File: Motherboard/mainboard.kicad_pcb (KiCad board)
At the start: 4 copper layers, 45 x 35 mm, 48 parts, among them IC1 BMX160, J1 Conn_01x01, J2 10118194-0001LF, J28 Conn_01x01, J29 Conn_01x01, J3 Micro_SD_Card, J30 Conn_01x01, J4 xf2m-2415-1a, J5 XF2M-1015-1A, SW1 KMR231NG LFS, U1 RFM95W-915S2, U2 ATSAMD51G_TQFN48, U3 DRV8848, U4 TPS82740BSIPR, U5 DRV8848, U6 MAX708RESA-T, U8 RFM95W-915S2, X1 ANTENNA_U.FL, X2 ANTENNA_U.FL

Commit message: put top layer back in after accidentally deleting it....
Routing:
- net +3V3: track 20.1 -> 21.6 mm, vias 15 -> 16
- added copper zone on F.Cu, net GND

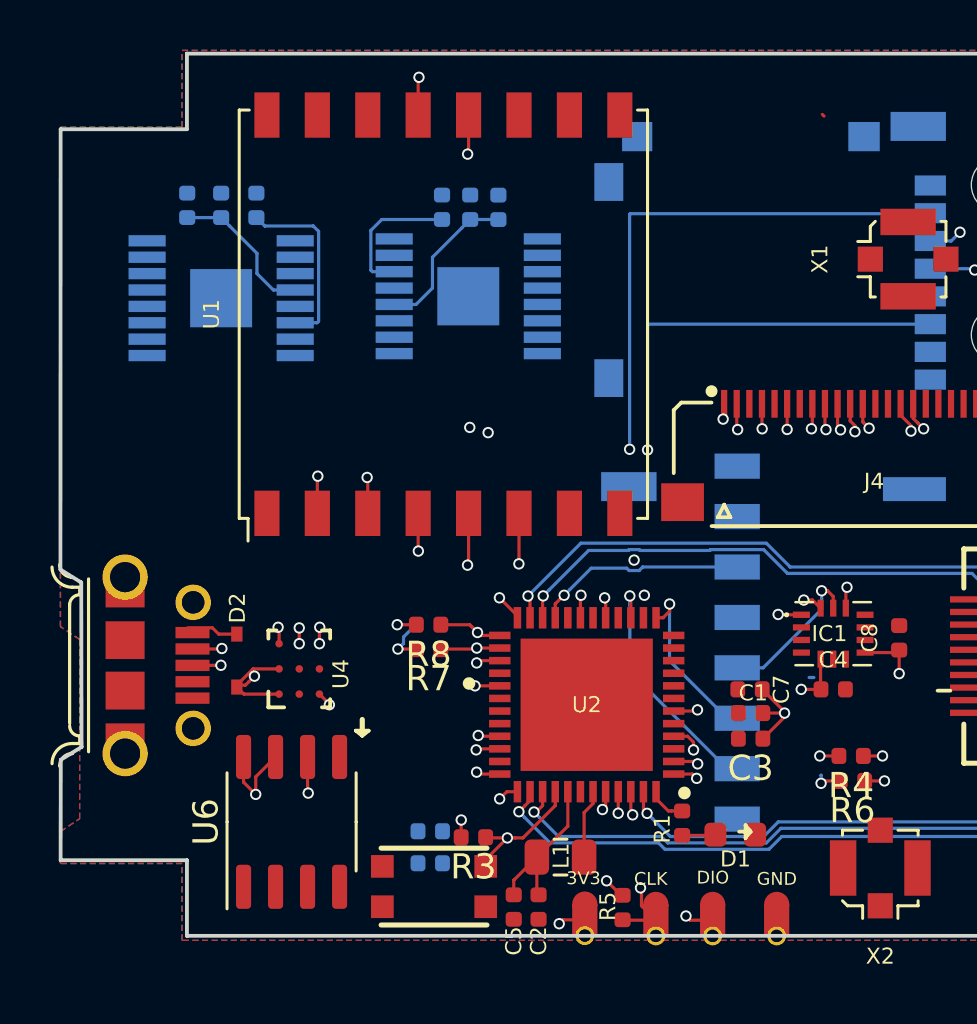
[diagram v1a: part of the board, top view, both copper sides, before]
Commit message: updated H-bridge voltage nests on schematic, updated traces on PCB for H-bridges to flat flex connector and for watchdog timer
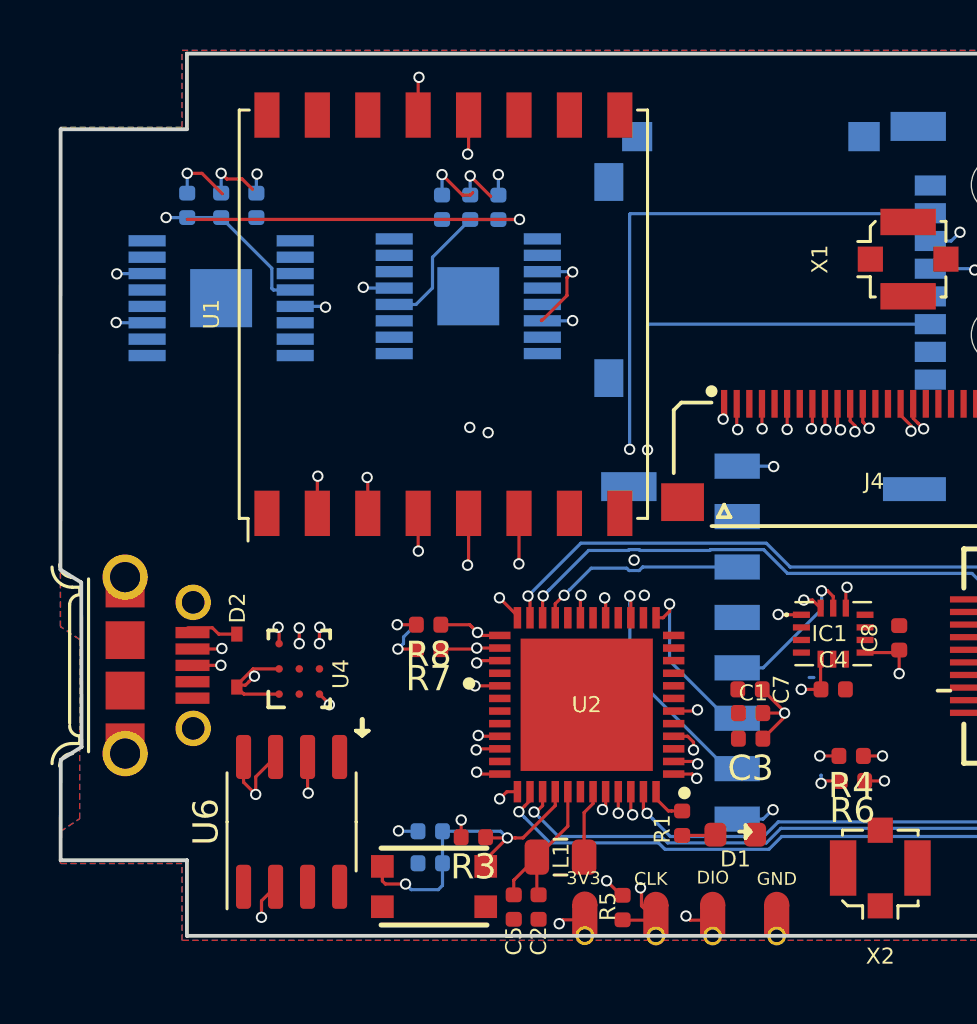
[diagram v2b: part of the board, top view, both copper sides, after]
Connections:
- C10 pad 1: Net-(C10-Pad1) -> BATT_P
- C11 pad 2: Net-(C11-Pad2) -> 3V3
- C12 pad 1: Net-(C12-Pad1) -> BATT_P
- C13 pad 2: Net-(C13-Pad2) -> 3V3
- C14 pad 1: Net-(C12-Pad1) -> BATT_P
- C9 pad 1: Net-(C10-Pad1) -> BATT_P
- U3 pad 11: VINT_1 -> 3V3
- U3 pad 12: Net-(C10-Pad1) -> BATT_P
- U3 pad 14: Net-(C11-Pad2) -> 3V3
- U5 pad 11: VINT_1 -> 3V3
- U5 pad 12: Net-(C12-Pad1) -> BATT_P
- U5 pad 14: Net-(C13-Pad2) -> 3V3
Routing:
- net BATT_P: track 13.9 -> 83.9 mm, vias 2 -> 4
- net GND: track 2.76 -> 27.4 mm, vias 2 -> 17
- net ~RESET: track 5.69 -> 13.7 mm, vias 1 -> 2
- net Net-(C13-Pad2): track 7.21 -> 0.00 mm
- net Net-(C10-Pad1): track 6.24 -> 0.00 mm
- net Net-(C12-Pad1): track 5.94 -> 0.00 mm
- net Net-(C11-Pad2): track 5.53 -> 0.00 mm
- net +3V3: track 21.6 -> 23.4 mm, vias 16 -> 17

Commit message: finished final touches for motherboard first draft
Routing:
- net BATT_P: track 83.9 -> 70.8 mm
- net 3V3: track 0.00 -> 2.23 mm, vias 0 -> 1
- net ~RESET: track 13.7 -> 15.0 mm
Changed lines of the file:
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@@
     (thickness 1.2)
     (drawings 35)
-    (tracks 629)
+    (tracks 634)
     (zones 0)
     (modules 48)
@@
   )
   (layers
-    (0 Top power hide)
-    (1 In1.Cu mixed)
+    (0 Top power)
+    (1 In1.Cu mixed hide)
     (2 In2.Cu mixed hide)
     (31 Bottom power)
@@
   (segment (start 91.86404 104.89184) (end 94.17304 104.89184) (width 0.127) (layer Bottom) (net 63))
   (segment (start 91.86404 105.74184) (end 91.86404 104.89184) (width 0.127) (layer Bottom) (net 63))
-  (via (at 90.3986 106.9848) (size 0.45) (drill 0.3) (layers Top Bottom) (net 63))
-  (segment (start 89.6003 106.9848) (end 90.3986 106.9848) (width 0.127) (layer Top) (net 63))
-  (segment (start 89.4789 106.8634) (end 89.6003 106.9848) (width 0.127) (layer Top) (net 63))
-  (segment (start 89.4789 106.2864) (end 89.4789 106.8634) (width 0.127) (layer Top) (net 63))
-  (segment (start 90.623599 107.209799) (end 91.697601 107.209799) (width 0.127) (layer Bottom) (net 63))
-  (segment (start 90.3986 106.9848) (end 90.623599 107.209799) (width 0.127) (layer Bottom) (net 63))
-  (segment (start 91.86404 107.04336) (end 91.86404 106.16184) (width 0.127) (layer Bottom) (net 63))
-  (segment (start 91.697601 107.209799) (end 91.86404 107.04336) (width 0.127) (layer Bottom) (net 63))
+  (via (at 91.8464 106.9086) (size 0.45) (drill 0.3) (layers Top Bottom) (net 63))
+  (segment (start 91.86404 106.89096) (end 91.8464 106.9086) (width 0.127) (layer Bottom) (net 63))
+  (segment (start 91.86404 106.16184) (end 91.86404 106.89096) (width 0.127) (layer Bottom) (net 63))
+  (segment (start 91.2242 106.2864) (end 89.4789 106.2864) (width 0.127) (layer Top) (net 63))
+  (segment (start 91.8464 106.9086) (end 91.2242 106.2864) (width 0.127) (layer Top) (net 63))
+  (segment (start 92.4686 106.2864) (end 93.5789 106.2864) (width 0.127) (layer Top) (net 63))
+  (segment (start 91.8464 106.9086) (end 92.4686 106.2864) (width 0.127) (layer Top) (net 63))
   (via (at 94.1324 103.6066) (size 0.45) (drill 0.3) (layers Top Bottom) (net 64))
   (segment (start 94.4162 103.3228) (end 94.1324 103.6066) (width 0.127) (layer Top) (net 64))
@@
   (segment (start 86.7664 103.6066) (end 86.5378 103.378) (width 0.127) (layer In1.Cu) (net 64))
   (segment (start 94.1324 103.6066) (end 86.7664 103.6066) (width 0.127) (layer In1.Cu) (net 64))
-  (via (at 113.9952 88.9254) (size 0.45) (drill 0.3) (layers Top Bottom) (net 67))
-  (segment (start 114.0382 88.8824) (end 113.9952 88.9254) (width 0.127) (layer Top) (net 67))
-  (segment (start 114.0382 87.9348) (end 114.0382 88.8824) (width 0.127) (layer Top) (net 67))
   (via (at 113.383737 98.663486) (size 0.45) (drill 0.3) (layers Top Bottom) (net 67))
   (segment (start 113.354823 98.6924) (end 113.383737 98.663486) (width 0.127) (layer Top) (net 67))
   (segment (start 112.5474 98.6924) (end 113.354823 98.6924) (width 0.127) (layer Top) (net 67))
-  (segment (start 113.701935 98.663486) (end 113.383737 98.663486) (width 0.127) (layer In2.Cu) (net 67))
-  (segment (start 113.750306 98.663486) (end 113.701935 98.663486) (width 0.127) (layer In2.Cu) (net 67))
-  (segment (start 113.9952 88.9254) (end 114.220199 89.150399) (width 0.127) (layer In2.Cu) (net 67))
-  (segment (start 114.220199 98.193593) (end 113.750306 98.663486) (width 0.127) (layer In2.Cu) (net 67))
-  (segment (start 114.220199 89.150399) (end 114.220199 98.193593) (width 0.127) (layer In2.Cu) (net 67))
-  (segment (start 114.5382 88.880779) (end 114.59261 88.935189) (width 0.127) (layer Top) (net 68))
-  (via (at 114.59261 88.935189) (size 0.45) (drill 0.3) (layers Top Bottom) (net 68))
-  (segment (start 114.5382 87.9348) (end 114.5382 88.880779) (width 0.127) (layer Top) (net 68))
-  (segment (start 114.59261 88.935189) (end 114.59261 99.331703) (width 0.127) (layer In2.Cu) (net 68))
-  (segment (start 113.821309 100.103004) (end 113.59631 100.328003) (width 0.127) (layer In2.Cu) (net 68))
+  (via (at 114.114123 88.918794) (size 0.45) (drill 0.3) (layers Top Bottom) (net 67))
+  (segment (start 114.220199 98.145222) (end 114.220199 89.343068) (width 0.127) (layer In2.Cu) (net 67))
+  (segment (start 114.0382 87.9348) (end 114.0382 88.842871) (width 0.127) (layer Top) (net 67))
+  (segment (start 114.0382 88.842871) (end 114.114123 88.918794) (width 0.127) (layer Top) (net 67))
+  (segment (start 113.383737 98.663486) (end 113.701935 98.663486) (width 0.127) (layer In2.Cu) (net 67))
+  (segment (start 113.701935 98.663486) (end 114.220199 98.145222) (width 0.127) (layer In2.Cu) (net 67))
+  (segment (start 114.114123 89.236992) (end 114.114123 88.918794) (width 0.127) (layer In2.Cu) (net 67))
+  (segment (start 114.220199 89.343068) (end 114.114123 89.236992) (width 0.127) (layer In2.Cu) (net 67))
   (via (at 113.59631 100.328003) (size 0.45) (drill 0.3) (layers Top Bottom) (net 68))
   (segment (start 113.460707 100.1924) (end 113.59631 100.328003) (width 0.127) (layer Top) (net 68))
-  (segment (start 114.59261 99.331703) (end 113.821309 100.103004) (width 0.127) (layer In2.Cu) (net 68))
   (segment (start 112.5474 100.1924) (end 113.460707 100.1924) (width 0.127) (layer Top) (net 68))
   (segment (start 94.0792 80.622) (end 94.0816 80.6244) (width 0.127) (layer Bottom) (net 68))
@@
   (segment (start 94.915 80.6244) (end 94.9198 80.6196) (width 0.127) (layer Bottom) (net 68))
   (segment (start 94.0816 80.6244) (end 94.915 80.6244) (width 0.127) (layer Bottom) (net 68))
-  (segment (start 94.9198 80.6196) (end 81.7372 80.6196) (width 0.127) (layer Top) (net 68))
   (via (at 80.899 80.5434) (size 0.45) (drill 0.3) (layers Top Bottom) (net 68))
   (segment (start 80.9014 80.5458) (end 80.899 80.5434) (width 0.127) (layer Bottom) (net 68))
   (segment (start 81.7372 80.5458) (end 80.9014 80.5458) (width 0.127) (layer Bottom) (net 68))
-  (segment (start 115.234901 88.292898) (end 115.234901 80.649899) (width 0.127) (layer In1.Cu) (net 68))
-  (segment (start 114.59261 88.935189) (end 115.234901 88.292898) (width 0.127) (layer In1.Cu) (net 68))
-  (segment (start 115.204602 80.6196) (end 94.9198 80.6196) (width 0.127) (layer In1.Cu) (net 68))
-  (segment (start 115.234901 80.649899) (end 115.204602 80.6196) (width 0.127) (layer In1.Cu) (net 68))
   (segment (start 92.9664 80.6244) (end 92.964 80.622) (width 0.127) (layer Bottom) (net 68))
   (segment (start 94.0816 80.6244) (end 92.9664 80.6244) (width 0.127) (layer Bottom) (net 68))
@@
   (segment (start 91.467299 83.339601) (end 90.8143 83.9926) (width 0.127) (layer Bottom) (net 68))
   (segment (start 92.964 80.622) (end 91.467299 82.118701) (width 0.127) (layer Bottom) (net 68))
+  (segment (start 113.59631 100.328003) (end 114.690797 99.233516) (width 0.127) (layer In2.Cu) (net 68))
+  (segment (start 115.204602 80.6196) (end 115.234901 80.649899) (width 0.127) (layer In1.Cu) (net 68))
+  (via (at 114.690797 88.938553) (size 0.45) (drill 0.3) (layers Top Bottom) (net 68))
+  (segment (start 115.234901 88.394449) (end 114.915796 88.713554) (width 0.127) (layer In1.Cu) (net 68))
+  (segment (start 114.690797 89.256751) (end 114.690797 88.938553) (width 0.127) (layer In2.Cu) (net 68))
+  (segment (start 114.5382 87.9348) (end 114.5382 88.785956) (width 0.127) (layer Top) (net 68))
+  (segment (start 115.234901 80.649899) (end 115.234901 88.394449) (width 0.127) (layer In1.Cu) (net 68))
+  (segment (start 114.915796 88.713554) (end 114.690797 88.938553) (width 0.127) (layer In1.Cu) (net 68))
+  (segment (start 114.5382 88.785956) (end 114.690797 88.938553) (width 0.127) (layer Top) (net 68))
+  (segment (start 114.690797 99.233516) (end 114.690797 89.256751) (width 0.127) (layer In2.Cu) (net 68))
+  (segment (start 94.9198 80.6196) (end 115.204602 80.6196) (width 0.127) (layer In1.Cu) (net 68))
   (segment (start 91.8406 97.6228) (end 91.8004 97.663) (width 0.127) (layer Top) (net 69))
   (via (at 93.223809 97.624144) (size 0.45) (drill 0.3) (layers Top Bottom) (net 69))
@@
   (segment (start 104.5382 88.9172) (end 104.5464 88.9254) (width 0.127) (layer Top) (net 79))
   (segment (start 104.5382 87.9348) (end 104.5382 88.9172) (width 0.127) (layer Top) (net 79))
+  (segment (start 113.5382 88.9506) (end 113.538 88.9508) (width 0.127) (layer Top) (net 81))
+  (via (at 113.538 88.9508) (size 0.45) (drill 0.3) (layers Top Bottom) (net 81))
+  (segment (start 113.5382 87.9348) (end 113.5382 88.9506) (width 0.127) (layer Top) (net 81))
+  (segment (start 91.8464 80.622) (end 91.0868 80.622) (width 0.127) (layer Bottom) (net 81))
+  (segment (start 84.9004 80.5458) (end 84.9234 80.5688) (width 0.127) (layer Bottom) (net 81))
+  (segment (start 84.4804 80.5458) (end 84.9004 80.5458) (width 0.127) (layer Bottom) (net 81))
   (via (at 93.1545 99.1235) (size 0.45) (drill 0.3) (layers Top Bottom) (net 82))
   (segment (start 93.1552 99.1228) (end 93.1545 99.1235) (width 0.127) (layer Top) (net 82))

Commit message: placement rework with 2019-10-23 mechanical updates
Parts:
- removed H1, H2, H3, H4: MountingHole, MountingHole:MountingHole_2.2mm_M2
- removed X1, X2: ANTENNA_U.FL, Connector_Coaxial:U.FL_Molex_MCRF_73412-0110_Vertical
- added C15: 0.1uF, Capacitor_SMD:C_0402_1005Metric, B.Cu at (93.3, 100.1)
- added J6: U.FL-R-SMT-1, custom-footprints:U.FL-R-SMT-1, B.Cu at (99.1, 105.2)
- added J7: U.FL-R-SMT-1, custom-footprints:U.FL-R-SMT-1, F.Cu at (98.8, 78.0)
- added REF**: U.FL_Hirose_U.FL-R-SMT-1_Vertical, Connector_Coaxial:U.FL_Hirose_U.FL-R-SMT-1_Vertical, F.Cu at (69.3, 102.6)
- C1, C2, C3, C5, C7, D1, L1, R1: moved to B.Cu
- moved J4 26.1 mm to (82.8, 85.7), turned to 270 degrees
- moved D1 24.3 mm to (79.5, 101.0), turned to 270 degrees
- moved R1 20.5 mm to (81.2, 101.0), turned to 270 degrees
- moved R8 19.6 mm to (72.3, 92.2)
- moved R7 19.4 mm to (72.4, 93.5)
- moved U1 19.1 mm to (111.0, 83.3), turned to 180 degrees
- moved C11 18.5 mm to (87.7, 62.1)
- moved C12 18.5 mm to (78.9, 62.0)
- moved C13 18.5 mm to (80.3, 62.0)
- moved C14 18.5 mm to (77.5, 62.0)
- moved C9 18.5 mm to (88.8, 62.1)
- moved U3 18.5 mm to (88.7, 65.6)
- moved U5 18.5 mm to (78.9, 65.7)
- moved C10 18.5 mm to (89.9, 62.1)
- moved J28 13.9 mm to (109.5, 118.1)
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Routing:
- net BATT_P: track 70.8 -> 0.00 mm, vias 4 -> 0
- net MISO: track 68.2 -> 0.00 mm, vias 5 -> 0
- net MOSI: track 57.7 -> 0.00 mm, vias 5 -> 0
- net SCK: track 48.7 -> 0.00 mm, vias 6 -> 0
- net GND: track 27.4 -> 0.00 mm, vias 17 -> 0
- net RF_DIO1: track 26.6 -> 0.00 mm, vias 1 -> 0
- net RF_DIO2: track 26.5 -> 0.00 mm, vias 1 -> 0
- net RF_BUSY: track 26.3 -> 0.00 mm, vias 1 -> 0
- net RF_DIO3: track 26.3 -> 0.00 mm, vias 1 -> 0
- net SDA1: track 25.2 -> 0.00 mm, vias 3 -> 0
- net SCL1: track 23.9 -> 0.00 mm, vias 3 -> 0
- net +3V3: track 23.4 -> 0.00 mm, vias 17 -> 0
- net EN_CAM: track 22.9 -> 0.00 mm, vias 2 -> 0
- net CS_CAM: track 22.7 -> 0.00 mm, vias 2 -> 0
- net RF_DIO0: track 22.6 -> 0.00 mm, vias 1 -> 0
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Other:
- board size 45 x 35 mm -> 45.2 x 36 mm
- net class Default: trace_width 0.127 -> 0.1524
